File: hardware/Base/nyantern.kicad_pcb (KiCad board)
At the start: 2 copper layers, 94 x 97.2 mm, 31 parts, among them U1 TP4056board, U3 WeMos_mini, U4 MPU6050board

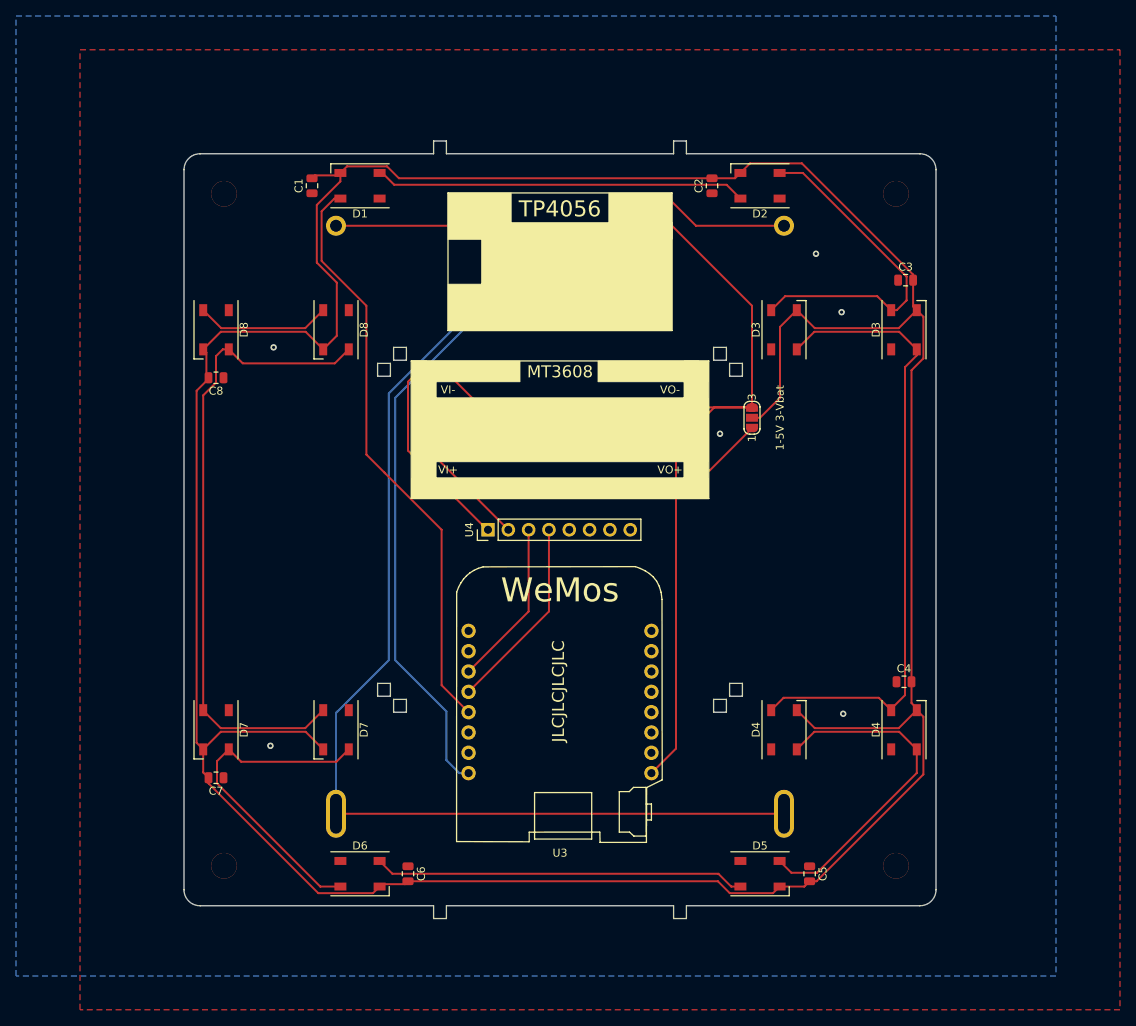
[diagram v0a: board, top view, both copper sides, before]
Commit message: Added reflective copper on inside Added version with cutout dinoskin Generated gerbers
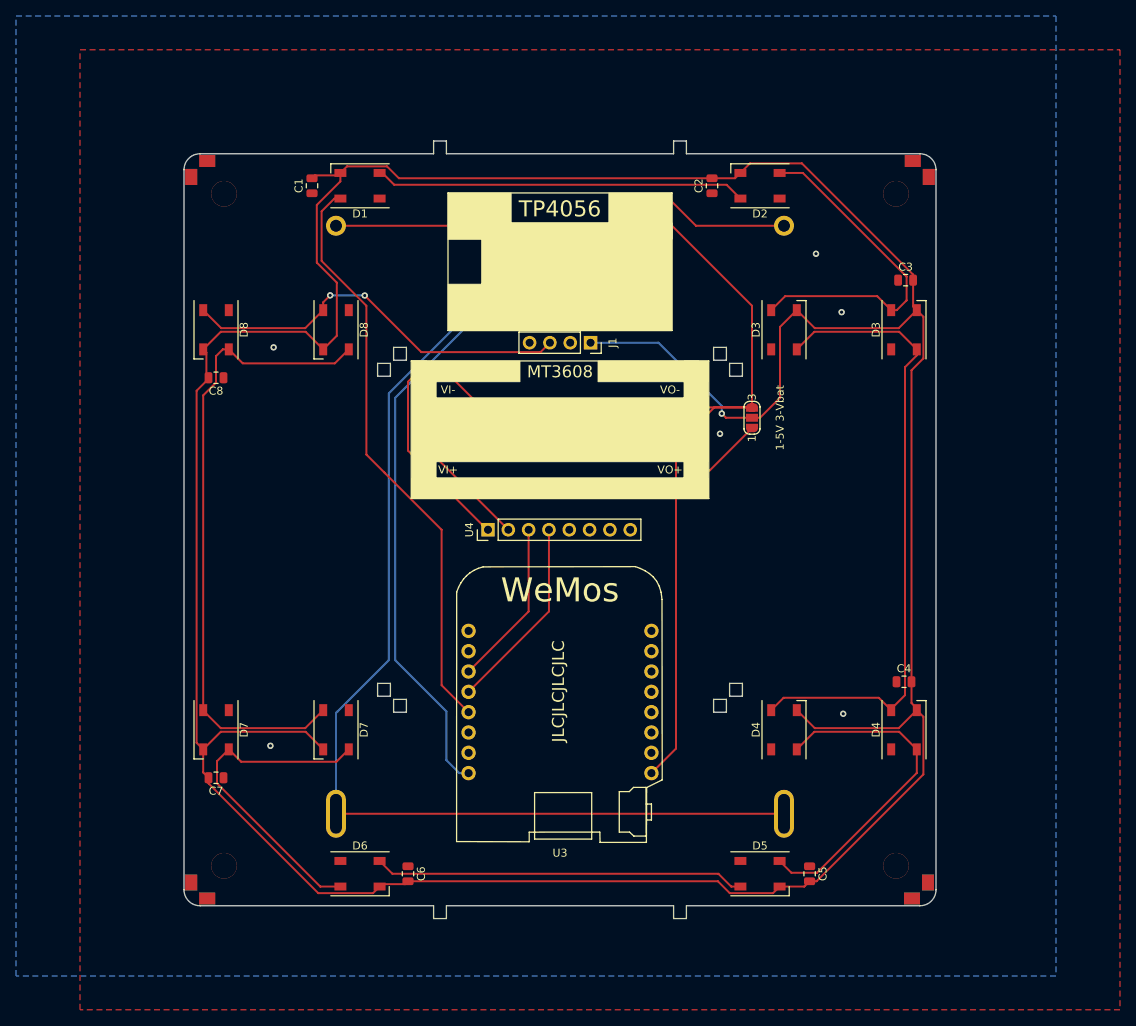
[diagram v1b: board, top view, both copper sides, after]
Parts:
- added J1: LED Panel Connector, Connector_PinSocket_2.54mm:PinSocket_1x04_P2.54mm_Vertical, F.Cu at (153.8, 76.6)
- added REF**: Center_Hole_Dial_2.05, BamboulabFootprints:Center_Hole_Dial_2.05, B.Cu at (196.1, 50.5)
- added REF**: Center_Hole_Dial_2.05, BamboulabFootprints:Center_Hole_Dial_2.05, F.Cu at (188.6, 146.1)
- added REF**: Center_Hole_Dial_2.05, BamboulabFootprints:Center_Hole_Dial_2.05, F.Cu at (100.5, 146.1)
- added REF**: Center_Hole_Dial_2.05, BamboulabFootprints:Center_Hole_Dial_2.05, F.Cu at (103.9, 138.7)
- added REF**: Center_Hole_Dial_2.05, BamboulabFootprints:Center_Hole_Dial_2.05, F.Cu at (199.5, 53.9)
- added REF**: Center_Hole_Dial_2.05, BamboulabFootprints:Center_Hole_Dial_2.05, F.Cu at (196.1, 61.3)
- added REF**: Center_Hole_Dial_2.05, BamboulabFootprints:Center_Hole_Dial_2.05, F.Cu at (103.9, 50.5)
- added REF**: Center_Hole_Dial_2.05, BamboulabFootprints:Center_Hole_Dial_2.05, F.Cu at (111.3, 53.9)
- added REF**: Center_Hole_Dial_2.05, BamboulabFootprints:Center_Hole_Dial_2.05, B.Cu at (188.7, 53.9)
- added REF**: Center_Hole_Dial_2.05, BamboulabFootprints:Center_Hole_Dial_2.05, B.Cu at (199.4, 146.1)
- added REF**: Center_Hole_Dial_2.05, BamboulabFootprints:Center_Hole_Dial_2.05, B.Cu at (196.0, 138.7)
- added REF**: Center_Hole_Dial_2.05, BamboulabFootprints:Center_Hole_Dial_2.05, B.Cu at (103.9, 149.5)
- added REF**: Center_Hole_Dial_2.05, BamboulabFootprints:Center_Hole_Dial_2.05, B.Cu at (111.3, 146.1)
- added REF**: Center_Hole_Dial_2.05, BamboulabFootprints:Center_Hole_Dial_2.05, B.Cu at (100.5, 53.9)
- added REF**: Center_Hole_Dial_2.05, BamboulabFootprints:Center_Hole_Dial_2.05, B.Cu at (103.9, 61.3)
- added REF**: Center_Hole_Dial_2.05, BamboulabFootprints:Center_Hole_Dial_2.05, F.Cu at (196.0, 149.5)
- renumbered e to U2
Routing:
- net Net-(D8-Pad4): track 16.9 -> 50.0 mm, vias 0 -> 2
- net Vdrive: track 413.9 -> 438.5 mm, vias 0 -> 1
